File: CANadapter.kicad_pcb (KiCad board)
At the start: 2 copper layers, 19 parts, among them P1 CONN_02X06, P2 CONN_01X06, P3 CONN_01X04, U1 MCP2515, U4 MCP2551-I/SN, U5 7805, Y1 16MHz

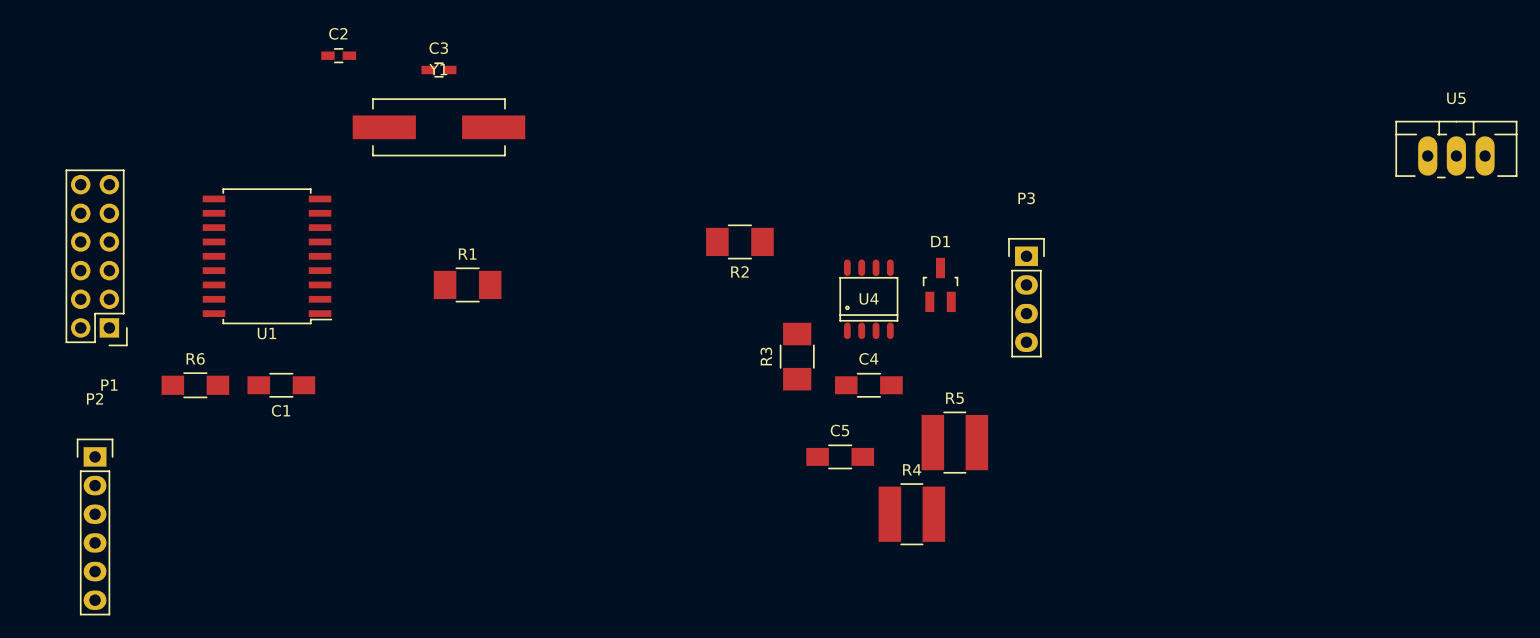
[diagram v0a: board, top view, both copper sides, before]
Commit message: corrected connectivity and pin numbering, placed parts
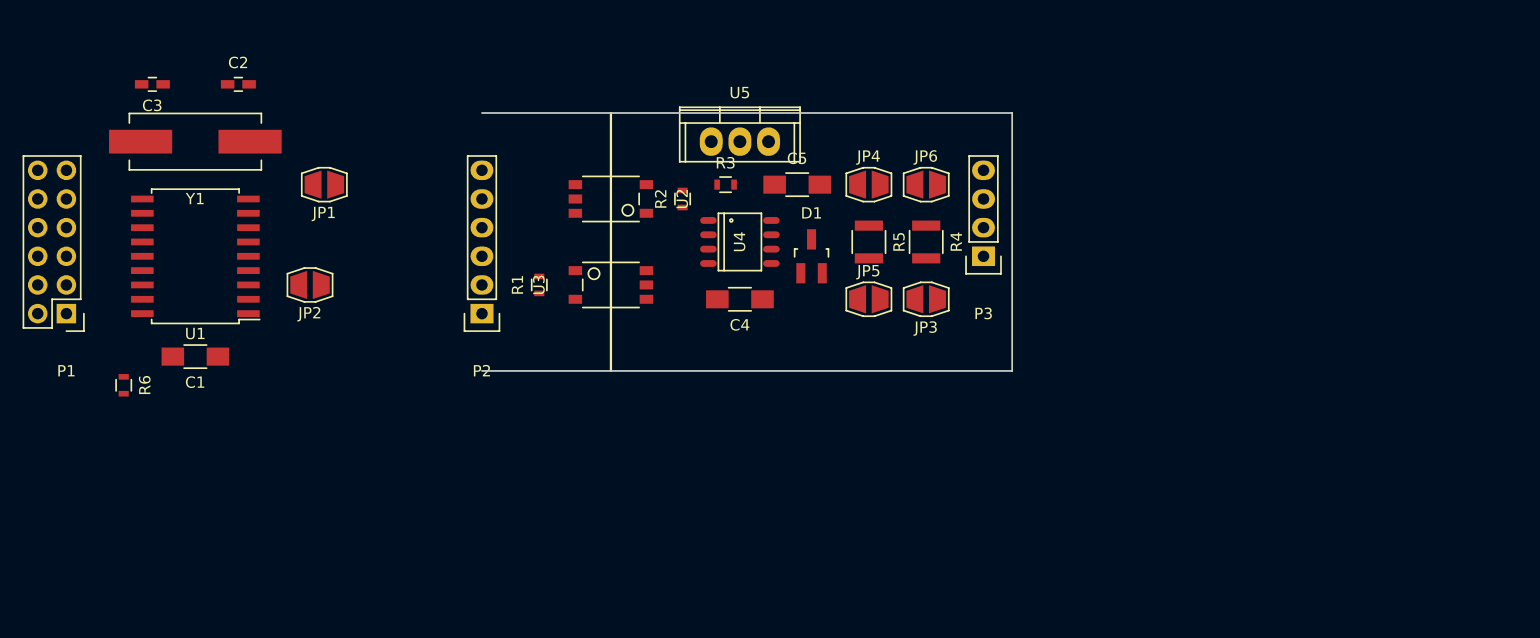
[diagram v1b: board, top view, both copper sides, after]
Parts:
- added JP1: Use MCP2515, LocalLib:JumperSingleJumbo, F.Cu at (119.4, 100.3)
- added JP2: Use MCP2515, LocalLib:JumperSingleJumbo, F.Cu at (118.1, 109.2)
- added JP3: Terminate, LocalLib:JumperSingleJumbo, F.Cu at (172.7, 110.5)
- added JP4: Filter, LocalLib:JumperSingleJumbo, F.Cu at (167.6, 100.3)
- added JP5: Terminate, LocalLib:JumperSingleJumbo, F.Cu at (167.6, 110.5)
- added JP6: Line Power, LocalLib:JumperSingleJumbo, F.Cu at (172.7, 100.3)
- added U2: TLP2361, LocalLib:soic-5, F.Cu at (144.8, 101.6)
- added U3: TLP2361, LocalLib:soic-5, F.Cu at (144.8, 109.2)
- R1, R2, R3: footprint Resistors_SMD:R_1210_HandSoldering -> Resistors_SMD:R_0603
- R4, R5: footprint Resistors_SMD:R_1218_HandSoldering -> Resistors_SMD:R_1210
- R6: footprint Resistors_SMD:R_1206_HandSoldering -> Resistors_SMD:R_0603
- U5: value 7805 -> LM7805CT; footprint TO_SOT_Packages_THT:TO-220_Neutral123_Vertical_LargePads -> Power_Integrations:TO-220
- moved U5 63.5 mm to (156.2, 96.5)
- moved P2 36.6 mm to (133.3, 111.8), turned to 180 degrees
- moved C3 25.4 mm to (104.1, 91.4), turned to 180 degrees
- moved C5 24.4 mm to (161.3, 100.3)
- moved R4 24.2 mm to (172.7, 105.4), turned to 270 degrees
- moved Y1 21.6 mm to (108.0, 96.5), turned to 180 degrees
- moved R5 19.3 mm to (167.6, 105.4), turned to 270 degrees
- moved R3 16.5 mm to (154.9, 100.3), turned to 0 degrees
- moved C4 13.7 mm to (156.2, 110.5), turned to 180 degrees
- moved U4 12.5 mm to (156.2, 105.4), turned to 270 degrees
- moved D1 11.7 mm to (162.6, 106.7)
- moved C2 9.25 mm to (111.8, 91.4)
- moved C1 8.03 mm to (108.0, 115.6)
- moved R2 6.35 mm to (151.1, 101.6), turned to 90 degrees
- moved R6 6.35 mm to (101.6, 118.1), turned to 270 degrees
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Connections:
- D1 pad 3: (no net) -> GNDREF
- P1 pad 6: Net-(P1-Pad6) -> (no net)
- P1 pad 8: Net-(P1-Pad8) -> (no net)
- P2 pad 1: Net-(P2-Pad1) -> (no net)
- P2 pad 4: Net-(P2-Pad4) -> (no net)
- U1 pad 10: Net-(U1-Pad10) -> (no net)
- U1 pad 11: Net-(U1-Pad11) -> (no net)
- U1 pad 3: Net-(U1-Pad3) -> (no net)
- U1 pad 4: Net-(U1-Pad4) -> (no net)
- U1 pad 5: Net-(U1-Pad5) -> (no net)
- U1 pad 6: Net-(U1-Pad6) -> (no net)
- U4 pad 5: Net-(U4-Pad5) -> (no net)
- U5 pad 1: (no net) -> +5V
- U5 pad 2: (no net) -> GNDREF
- U5 pad 3: (no net) -> Net-(JP6-Pad2)
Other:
- board outline added: 47 x 22.9 mm

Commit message: Partial layout
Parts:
- moved U2 7.62 mm to (144.8, 109.2)
- moved U3 7.62 mm to (144.8, 101.6)
- moved R2 5.75 mm to (150.5, 107.3), turned to 270 degrees
- moved R3 1.27 mm to (156.2, 100.3)
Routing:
- net GNDREF: track 0.00 -> 53.9 mm
- net /CAN_H: track 0.00 -> 30.4 mm
- net +5V: track 0.00 -> 29.7 mm
- net /CAN_L: track 0.00 -> 28.2 mm
- net Net-(JP6-Pad2): track 0.00 -> 16.6 mm
- net Net-(JP4-Pad1): track 0.00 -> 9.12 mm
- net Net-(U3-Pad5): track 0.00 -> 6.28 mm
- net +12V: track 0.00 -> 4.61 mm
- net Net-(R3-Pad2): track 0.00 -> 4.28 mm
- net Net-(JP5-Pad2): track 0.00 -> 4.04 mm
- net Net-(JP3-Pad1): track 0.00 -> 4.04 mm
- net Net-(C5-Pad2): track 0.00 -> 3.35 mm
- net Net-(R2-Pad1): track 0.00 -> 3.23 mm
- net Net-(R2-Pad2): track 0.00 -> 2.61 mm

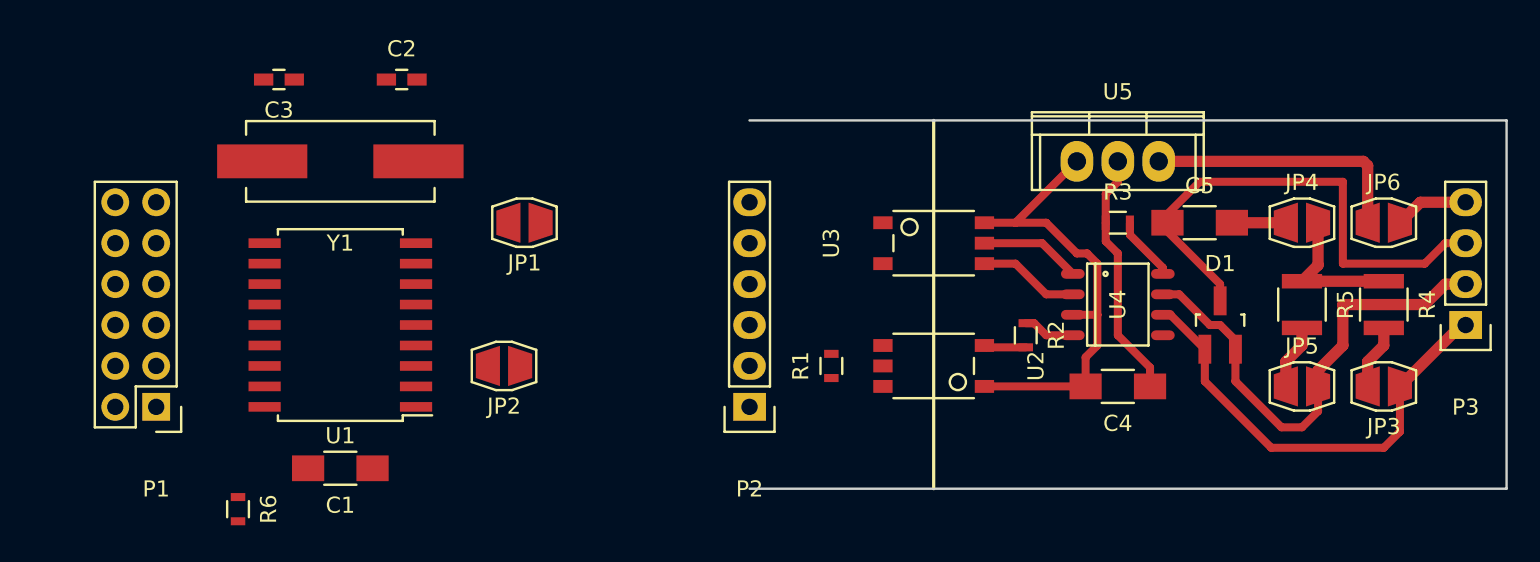
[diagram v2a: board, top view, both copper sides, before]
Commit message: substituted footprints, layout first pass complete
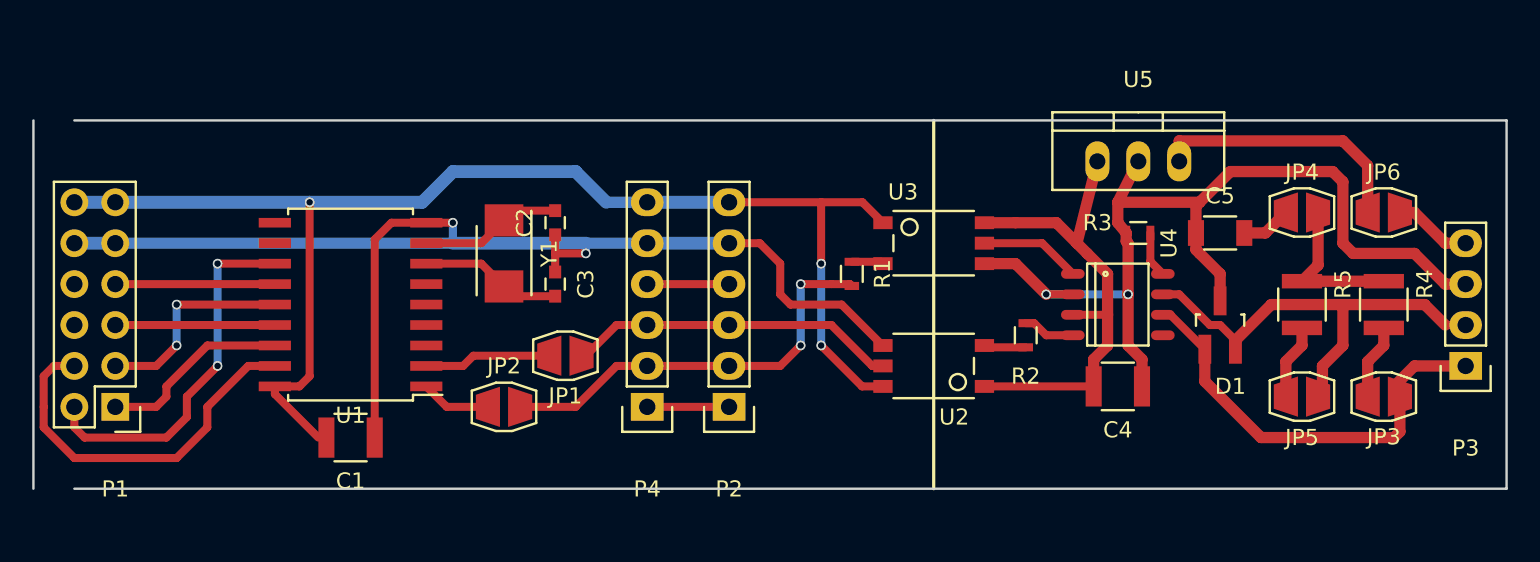
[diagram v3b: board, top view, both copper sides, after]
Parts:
- removed R6: 10K, Resistors_SMD:R_0603
- added P4: CONN_01X06, Pin_Headers:Pin_Header_Straight_1x06, F.Cu at (127.0, 111.8)
- C1, C4: footprint Capacitors_SMD:C_1206_HandSoldering -> Capacitors_SMD:C_1210
- C2, C3: footprint Capacitors_SMD:C_0603_HandSoldering -> Capacitors_SMD:C_0603
- C5: footprint Capacitors_SMD:C_1206_HandSoldering -> Capacitors_SMD:C_1206
- U5: footprint Power_Integrations:TO-220 -> TO_SOT_Packages_THT:TO-220_Neutral123_Vertical
- Y1: footprint Crystals:Crystal_HC49-SD_SMD -> Crystals:Crystal_SMD_5032_2Pads
- moved C3 21.3 mm to (121.3, 104.1), turned to 270 degrees
- moved C2 13.0 mm to (121.3, 100.3), turned to 90 degrees
- moved Y1 11.7 mm to (118.1, 102.2), turned to 270 degrees
- moved JP1 8.64 mm to (121.9, 108.6)
- moved R1 5.85 mm to (139.7, 103.5), turned to 270 degrees
- moved JP2 2.54 mm to (118.1, 111.8)
- moved P1 2.54 mm to (94.0, 111.8)
- moved P3 2.54 mm to (177.8, 109.2)
- moved C1 2.01 mm to (108.6, 113.7)
- moved C5 1.42 mm to (162.6, 101.0)
- moved U1 1.42 mm to (108.6, 105.4)
- moved R3 1.42 mm to (157.5, 101.0)
- moved P2 1.27 mm to (132.1, 111.8)
- moved U5 1.27 mm to (157.5, 96.5)
- moved JP3 0.64 mm to (172.7, 111.1)
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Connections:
- P2 pad 1: (no net) -> Net-(P2-Pad1)
- P2 pad 4: (no net) -> Net-(P2-Pad4)
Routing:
- net +3V3: track 0.00 -> 83.6 mm, vias 0 -> 3
- net GND: track 0.00 -> 77.7 mm, vias 0 -> 2
- net /CAN_TX: track 0.00 -> 26.0 mm, vias 0 -> 2
- net /~RST: track 0.00 -> 23.6 mm
- net /~INT: track 0.00 -> 22.9 mm, vias 0 -> 2
- net /CAN_RX: track 0.00 -> 20.6 mm
- net /MOSI: track 0.00 -> 13.0 mm, vias 0 -> 2
- net /CS: track 0.00 -> 11.9 mm
- net /SCK: track 0.00 -> 9.91 mm
- net /MISO: track 0.00 -> 9.91 mm
- net Net-(C3-Pad2): track 0.00 -> 8.84 mm
- net Net-(C2-Pad2): track 0.00 -> 8.84 mm
- net Net-(JP1-Pad1): track 0.00 -> 7.90 mm
- net GNDREF: track 53.9 -> 60.6 mm, vias 0 -> 2
- net Net-(P2-Pad4): track 0.00 -> 5.08 mm
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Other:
- board size 47 x 22.9 mm -> 91.4 x 22.9 mm

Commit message: added isolating smps, moved jumpers, added ground pours
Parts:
- added U6: NKE0305SC, LocalLib:Murata_SIL, F.Cu at (146.1, 96.5)
- moved JP2 10.2 mm to (128.3, 110.5)
- moved JP1 7.10 mm to (128.3, 105.4)
- moved P1 2.54 mm to (91.4, 111.8)
- moved P4 2.54 mm to (124.5, 111.8)
- moved Y1 2.54 mm to (115.6, 102.2)
- moved C1 2.54 mm to (106.0, 113.7)
- moved C2 2.54 mm to (118.7, 100.3)
- moved C3 2.54 mm to (118.7, 104.1)
- moved U1 2.54 mm to (106.0, 105.4)
- moved U2 1.27 mm to (146.1, 109.2)
- moved U3 1.27 mm to (146.1, 101.6)
- moved R2 0.90 mm to (151.1, 108.0)
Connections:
- JP1 pad 1: Net-(JP1-Pad1) -> /CAN_RX_C
- JP1 pad 2: /CAN_RX -> /CAN_RX_I
- JP2 pad 1: Net-(JP2-Pad1) -> /CAN_TX_C
- JP2 pad 2: /CAN_TX -> /CAN_TX_I
- P2 pad 1: Net-(P2-Pad1) -> (no net)
- P2 pad 2: /CAN_TX -> /CAN_TX_I
- P2 pad 3: /CAN_RX -> /CAN_RX_I
- P2 pad 4: Net-(P2-Pad4) -> (no net)
- P4 pad 1: Net-(P2-Pad1) -> (no net)
- P4 pad 2: /CAN_TX -> /CAN_TX_C
- P4 pad 3: /CAN_RX -> /CAN_RX_C
- P4 pad 4: Net-(P2-Pad4) -> (no net)
- R1 pad 2: /CAN_TX -> /CAN_TX_I
- U1 pad 1: Net-(JP2-Pad1) -> /CAN_TX_C
- U1 pad 2: Net-(JP1-Pad1) -> /CAN_RX_C
- U2 pad 5: /CAN_RX -> /CAN_RX_I
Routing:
- net /CAN_TX: track 26.0 -> 0.00 mm, vias 2 -> 0
- net /CAN_RX: track 20.6 -> 0.00 mm
- net /CAN_RX_C: track 0.00 -> 18.1 mm
- net /CAN_TX_C: track 0.00 -> 17.6 mm
- net GND: track 77.7 -> 94.1 mm, vias 2 -> 3
- net /CAN_RX_I: track 0.00 -> 15.2 mm
- net /CAN_TX_I: track 0.00 -> 15.2 mm, vias 0 -> 2
- net GNDREF: track 60.6 -> 75.3 mm, vias 2 -> 3
- net +3V3: track 83.6 -> 93.6 mm, vias 3 -> 4
- net Net-(JP1-Pad1): track 7.90 -> 0.00 mm
- net Net-(P2-Pad4): track 5.08 -> 0.00 mm
- net Net-(P2-Pad1): track 5.08 -> 0.00 mm
- net Net-(JP2-Pad1): track 4.35 -> 0.00 mm
- net +5V: track 30.5 -> 32.9 mm
- net Net-(R1-Pad1): track 1.98 -> 3.25 mm
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- added copper zone on B.Cu, net GND
- added copper zone on B.Cu, net GNDREF
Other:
- board size 91.4 x 22.9 mm -> 94 x 22.9 mm
- board text added: "+"
- board text added: "-"
- board text added: "3V3"
- board text added: "CAN GND"
- board text added: "CAN HIGH"
- board text added: "CAN LOW"
- board text added: "CAN RX"
- board text added: "CAN TX"
- board text added: "CAN V+"
- board text added: "CS"
- board text added: "Controller"
- board text added: "GND"
- board text added: "H"
- board text added: "INT"
- board text added: "Interface"
- board text added: "Isolation"
- board text added: "L"
- board text added: "MISO"
- board text added: "MOSI"
- board text added: "RST"
- board text added: "RX"
- board text added: "SCK"
- board text added: "TX"
